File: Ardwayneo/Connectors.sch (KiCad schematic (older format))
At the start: 4 parts

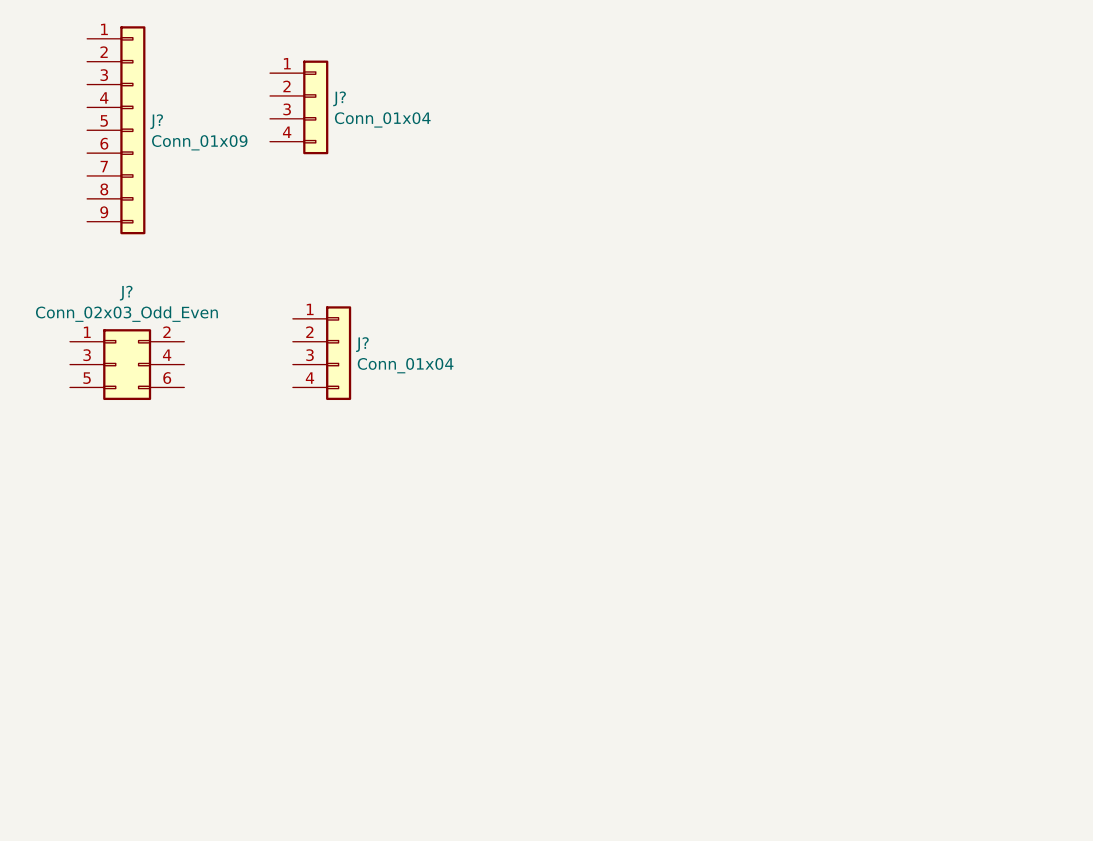
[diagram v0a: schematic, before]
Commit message: Annotation
Annotated all symbols
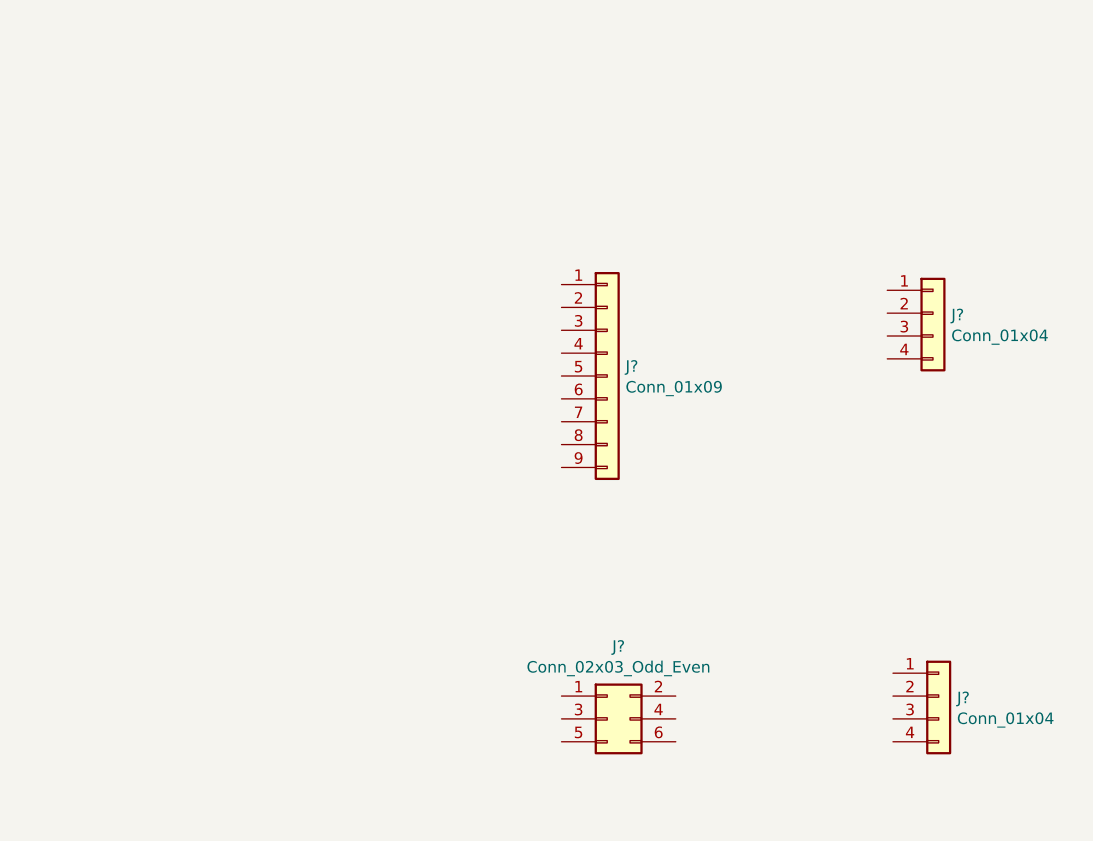
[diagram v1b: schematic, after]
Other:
- moved on the sheet: J?
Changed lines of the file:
@@
 L Connector_Generic:Conn_01x09 J?
 U 1 1 5FF1DD56
-P 3025 2225
-F 0 "J?" H 3105 2267 50  0000 L CNN
-F 1 "Conn_01x09" H 3105 2176 50  0000 L CNN
-F 2 "" H 3025 2225 50  0001 C CNN
-F 3 "~" H 3025 2225 50  0001 C CNN
-	1    3025 2225
+P 5100 3300
+F 0 "J?" H 5180 3342 50  0000 L CNN
+F 1 "Conn_01x09" H 5180 3251 50  0000 L CNN
+F 2 "" H 5100 3300 50  0001 C CNN
+F 3 "~" H 5100 3300 50  0001 C CNN
+	1    5100 3300
 	1    0    0    -1
 $EndComp
@@
 L Connector_Generic:Conn_01x04 J?
 U 1 1 5FF1EB6D
-P 3825 2075
-F 0 "J?" H 3905 2067 50  0000 L CNN
-F 1 "Conn_01x04" H 3905 1976 50  0000 L CNN
-F 2 "" H 3825 2075 50  0001 C CNN
-F 3 "~" H 3825 2075 50  0001 C CNN
-	1    3825 2075
+P 6525 3025
+F 0 "J?" H 6605 3017 50  0000 L CNN
+F 1 "Conn_01x04" H 6605 2926 50  0000 L CNN
+F 2 "" H 6525 3025 50  0001 C CNN
+F 3 "~" H 6525 3025 50  0001 C CNN
+	1    6525 3025
 	1    0    0    -1
 $EndComp
@@
 L Connector_Generic:Conn_02x03_Odd_Even J?
 U 1 1 5FF200E2
-P 2950 3250
-F 0 "J?" H 3000 3567 50  0000 C CNN
-F 1 "Conn_02x03_Odd_Even" H 3000 3476 50  0000 C CNN
-F 2 "" H 2950 3250 50  0001 C CNN
-F 3 "~" H 2950 3250 50  0001 C CNN
-	1    2950 3250
+P 5100 4800
+F 0 "J?" H 5150 5117 50  0000 C CNN
+F 1 "Conn_02x03_Odd_Even" H 5150 5026 50  0000 C CNN
+F 2 "" H 5100 4800 50  0001 C CNN
+F 3 "~" H 5100 4800 50  0001 C CNN
+	1    5100 4800
 	1    0    0    -1
 $EndComp
@@
 L Connector_Generic:Conn_01x04 J?
 U 1 1 5FF21B9C
-P 3925 3150
-F 0 "J?" H 4005 3142 50  0000 L CNN
-F 1 "Conn_01x04" H 4005 3051 50  0000 L CNN
-F 2 "" H 3925 3150 50  0001 C CNN
-F 3 "~" H 3925 3150 50  0001 C CNN
-	1    3925 3150
+P 6550 4700
+F 0 "J?" H 6630 4692 50  0000 L CNN
+F 1 "Conn_01x04" H 6630 4601 50  0000 L CNN
+F 2 "" H 6550 4700 50  0001 C CNN
+F 3 "~" H 6550 4700 50  0001 C CNN
+	1    6550 4700
 	1    0    0    -1
 $EndComp

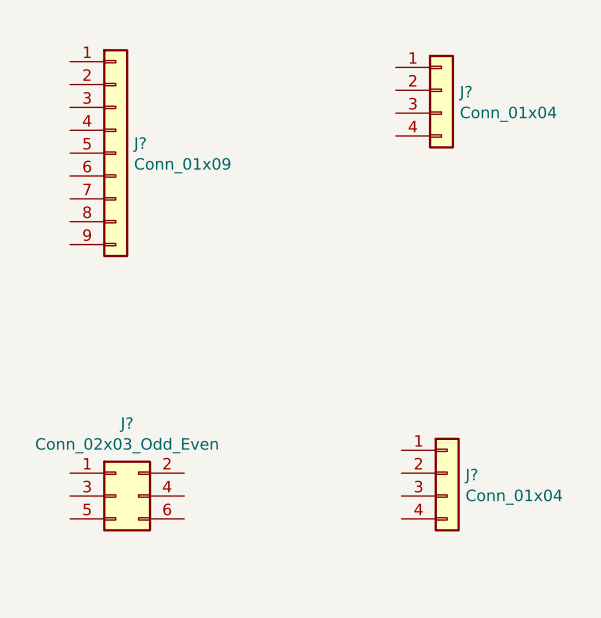
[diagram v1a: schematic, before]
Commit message: Added sheet connector pins to ATMEGA
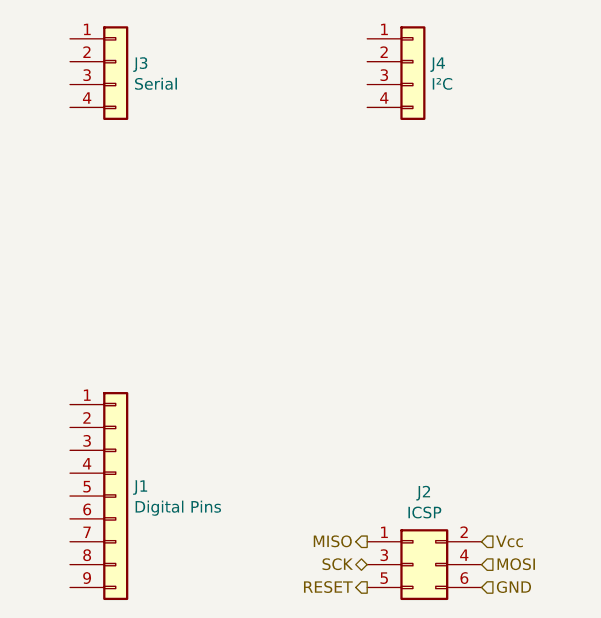
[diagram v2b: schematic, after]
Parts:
- J1: renamed from J?; value Conn_01x09 -> Digital Pins; footprint (none) -> Connector_PinHeader_2.54mm:PinHeader_1x09_P2.54mm_Vertical
- J2: renamed from J?; value Conn_02x03_Odd_Even -> ICSP; footprint (none) -> Connector_PinSocket_2.54mm:PinSocket_2x03_P2.54mm_Vertical
- J3: renamed from J?; value Conn_01x04 -> Serial; footprint (none) -> Connector_PinSocket_2.54mm:PinSocket_1x04_P2.54mm_Vertical
- J4: renamed from J?; value Conn_01x04 -> I²C; footprint (none) -> Connector_PinSocket_2.54mm:PinSocket_1x04_P2.54mm_Vertical
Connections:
- net MISO: now reaches J2.1 (Pin_1)
- net Vcc: now reaches J2.2 (Pin_2)
- net SCK: now reaches J2.3 (Pin_3)
- net MOSI: now reaches J2.4 (Pin_4)
- net RESET: now reaches J2.5 (Pin_5)
- net GND: now reaches J2.6 (Pin_6)
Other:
- moved on the sheet: J1, J2, J3, J4
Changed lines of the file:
@@
 $EndDescr
 $Comp
-L Connector_Generic:Conn_01x09 J?
+L Connector_Generic:Conn_01x09 J1
 U 1 1 5FF1DD56
-P 5100 3300
-F 0 "J?" H 5180 3342 50  0000 L CNN
-F 1 "Conn_01x09" H 5180 3251 50  0000 L CNN
-F 2 "" H 5100 3300 50  0001 C CNN
-F 3 "~" H 5100 3300 50  0001 C CNN
-	1    5100 3300
-	1    0    0    -1
-$EndComp
-$Comp
-L Connector_Generic:Conn_01x04 J?
-U 1 1 5FF1EB6D
-P 6525 3025
-F 0 "J?" H 6605 3017 50  0000 L CNN
-F 1 "Conn_01x04" H 6605 2926 50  0000 L CNN
-F 2 "" H 6525 3025 50  0001 C CNN
-F 3 "~" H 6525 3025 50  0001 C CNN
-	1    6525 3025
-	1    0    0    -1
-$EndComp
-$Comp
-L Connector_Generic:Conn_02x03_Odd_Even J?
-U 1 1 5FF200E2
 P 5100 4800
-F 0 "J?" H 5150 5117 50  0000 C CNN
-F 1 "Conn_02x03_Odd_Even" H 5150 5026 50  0000 C CNN
-F 2 "" H 5100 4800 50  0001 C CNN
+F 0 "J1" H 5180 4842 50  0000 L CNN
+F 1 "Digital Pins" H 5180 4751 50  0000 L CNN
+F 2 "Connector_PinHeader_2.54mm:PinHeader_1x09_P2.54mm_Vertical" H 5100 4800 50  0001 C CNN
 F 3 "~" H 5100 4800 50  0001 C CNN
 	1    5100 4800
@@
 $EndComp
 $Comp
-L Connector_Generic:Conn_01x04 J?
-U 1 1 5FF21B9C
-P 6550 4700
-F 0 "J?" H 6630 4692 50  0000 L CNN
-F 1 "Conn_01x04" H 6630 4601 50  0000 L CNN
-F 2 "" H 6550 4700 50  0001 C CNN
-F 3 "~" H 6550 4700 50  0001 C CNN
-	1    6550 4700
+L Connector_Generic:Conn_01x04 J3
+U 1 1 5FF1EB6D
+P 5100 2900
+F 0 "J3" H 5180 2892 50  0000 L CNN
+F 1 "Serial" H 5180 2801 50  0000 L CNN
+F 2 "Connector_PinSocket_2.54mm:PinSocket_1x04_P2.54mm_Vertical" H 5100 2900 50  0001 C CNN
+F 3 "~" H 5100 2900 50  0001 C CNN
+	1    5100 2900
 	1    0    0    -1
 $EndComp
+$Comp
+L Connector_Generic:Conn_02x03_Odd_Even J2
+U 1 1 5FF200E2
+P 6400 5100
+F 0 "J2" H 6450 5417 50  0000 C CNN
+F 1 "ICSP" H 6450 5326 50  0000 C CNN
+F 2 "Connector_PinSocket_2.54mm:PinSocket_2x03_P2.54mm_Vertical" H 6400 5100 50  0001 C CNN
+F 3 "~" H 6400 5100 50  0001 C CNN
+	1    6400 5100
+	1    0    0    -1
+$EndComp
+$Comp
+L Connector_Generic:Conn_01x04 J4
+U 1 1 5FF21B9C
+P 6400 2900
+F 0 "J4" H 6480 2892 50  0000 L CNN
+F 1 "I²C" H 6480 2801 50  0000 L CNN
+F 2 "Connector_PinSocket_2.54mm:PinSocket_1x04_P2.54mm_Vertical" H 6400 2900 50  0001 C CNN
+F 3 "~" H 6400 2900 50  0001 C CNN
+	1    6400 2900
+	1    0    0    -1
+$EndComp
+Text HLabel 6200 5000 0    50   Output ~ 0
+MISO
+Text HLabel 6200 5100 0    50   BiDi ~ 0
+SCK
+Text HLabel 6200 5200 0    50   Output ~ 0
+RESET
+Text HLabel 6700 5000 2    50   Input ~ 0
+Vcc
+Text HLabel 6700 5100 2    50   Input ~ 0
+MOSI
+Text HLabel 6700 5200 2    50   Input ~ 0
+GND
 $EndSCHEMATC

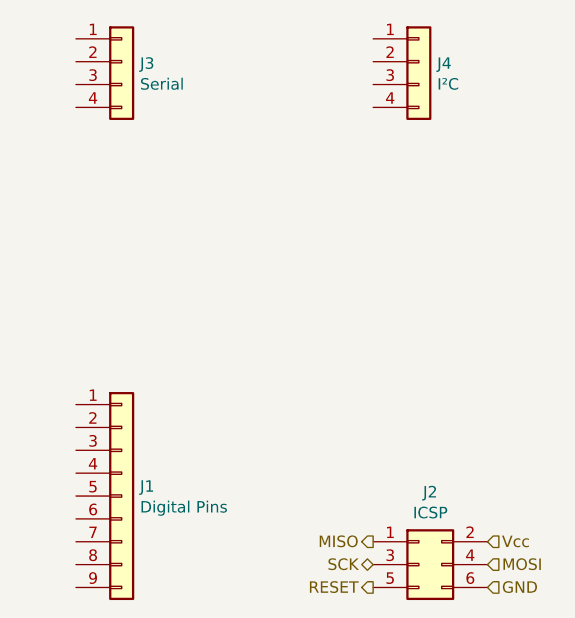
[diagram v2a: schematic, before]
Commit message: Completed wiring from connectors sheet
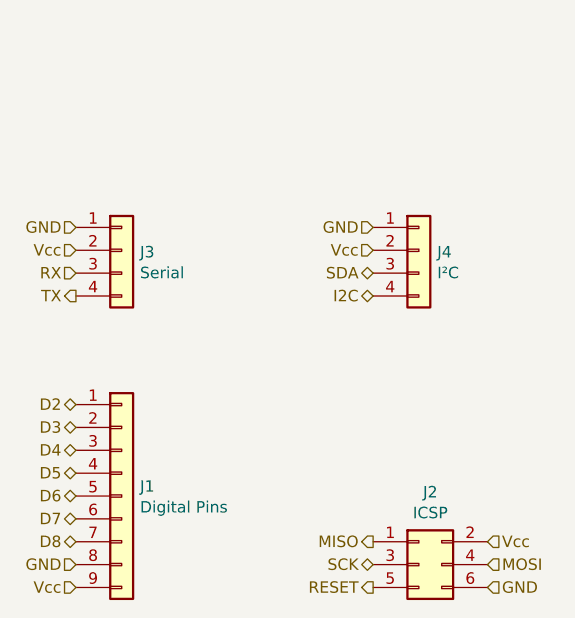
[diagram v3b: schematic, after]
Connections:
- net GND: now also J1.8 (Pin_8), J3.1 (Pin_1), J4.1 (Pin_1)
- net Vcc: now also J1.9 (Pin_9), J3.2 (Pin_2), J4.2 (Pin_2)
- net D2: now reaches J1.1 (Pin_1)
- net D3: now reaches J1.2 (Pin_2)
- net D4: now reaches J1.3 (Pin_3)
- net D5: now reaches J1.4 (Pin_4)
- net D6: now reaches J1.5 (Pin_5)
- net D7: now reaches J1.6 (Pin_6)
- net D8: now reaches J1.7 (Pin_7)
- net RX: now reaches J3.3 (Pin_3)
- net TX: now reaches J3.4 (Pin_4)
- net SDA: now reaches J4.3 (Pin_3)
- net I2C: now reaches J4.4 (Pin_4)
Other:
- moved on the sheet: J3, J4
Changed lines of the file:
@@
 L Connector_Generic:Conn_01x04 J3
 U 1 1 5FF1EB6D
-P 5100 2900
-F 0 "J3" H 5180 2892 50  0000 L CNN
-F 1 "Serial" H 5180 2801 50  0000 L CNN
-F 2 "Connector_PinSocket_2.54mm:PinSocket_1x04_P2.54mm_Vertical" H 5100 2900 50  0001 C CNN
-F 3 "~" H 5100 2900 50  0001 C CNN
-	1    5100 2900
+P 5100 3725
+F 0 "J3" H 5180 3717 50  0000 L CNN
+F 1 "Serial" H 5180 3626 50  0000 L CNN
+F 2 "Connector_PinSocket_2.54mm:PinSocket_1x04_P2.54mm_Vertical" H 5100 3725 50  0001 C CNN
+F 3 "~" H 5100 3725 50  0001 C CNN
+	1    5100 3725
 	1    0    0    -1
 $EndComp
@@
 F 3 "~" H 6400 5100 50  0001 C CNN
 	1    6400 5100
-	1    0    0    -1
-$EndComp
-$Comp
-L Connector_Generic:Conn_01x04 J4
-U 1 1 5FF21B9C
-P 6400 2900
-F 0 "J4" H 6480 2892 50  0000 L CNN
-F 1 "I²C" H 6480 2801 50  0000 L CNN
-F 2 "Connector_PinSocket_2.54mm:PinSocket_1x04_P2.54mm_Vertical" H 6400 2900 50  0001 C CNN
-F 3 "~" H 6400 2900 50  0001 C CNN
-	1    6400 2900
 	1    0    0    -1
 $EndComp
@@
 Text HLabel 6700 5200 2    50   Input ~ 0
 GND
+Text HLabel 4900 3625 0    50   Input ~ 0
+GND
+Text HLabel 4900 3725 0    50   Input ~ 0
+Vcc
+Text HLabel 4900 3825 0    50   Input ~ 0
+RX
+Text HLabel 4900 3925 0    50   Output ~ 0
+TX
+Text HLabel 6200 3625 0    50   Input ~ 0
+GND
+Text HLabel 6200 3725 0    50   Input ~ 0
+Vcc
+Text HLabel 6200 3825 0    50   BiDi ~ 0
+SDA
+Text HLabel 6200 3925 0    50   BiDi ~ 0
+I2C
+Text HLabel 4900 4400 0    50   BiDi ~ 0
+D2
+Text HLabel 4900 4500 0    50   BiDi ~ 0
+D3
+Text HLabel 4900 4600 0    50   BiDi ~ 0
+D4
+Text HLabel 4900 4700 0    50   BiDi ~ 0
+D5
+Text HLabel 4900 4800 0    50   BiDi ~ 0
+D6
+Text HLabel 4900 4900 0    50   BiDi ~ 0
+D7
+Text HLabel 4900 5000 0    50   BiDi ~ 0
+D8
+Text HLabel 4900 5100 0    50   Input ~ 0
+GND
+Text HLabel 4900 5200 0    50   Input ~ 0
+Vcc
+$Comp
+L Connector_Generic:Conn_01x04 J4
+U 1 1 5FF21B9C
+P 6400 3725
+F 0 "J4" H 6480 3717 50  0000 L CNN
+F 1 "I²C" H 6480 3626 50  0000 L CNN
+F 2 "Connector_PinSocket_2.54mm:PinSocket_1x04_P2.54mm_Vertical" H 6400 3725 50  0001 C CNN
+F 3 "~" H 6400 3725 50  0001 C CNN
+	1    6400 3725
+	1    0    0    -1
+$EndComp
 $EndSCHEMATC

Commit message: Completed all wiring
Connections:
- net I2C is gone; now on net SCK: J4.4 (Pin_4)
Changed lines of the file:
@@
 SDA
 Text HLabel 6200 3925 0    50   BiDi ~ 0
-I2C
+SCK
 Text HLabel 4900 4400 0    50   BiDi ~ 0
 D2

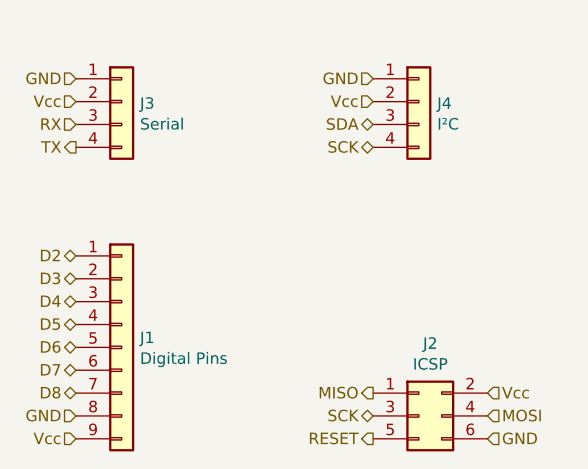
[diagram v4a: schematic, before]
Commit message: Added functional block descriptions
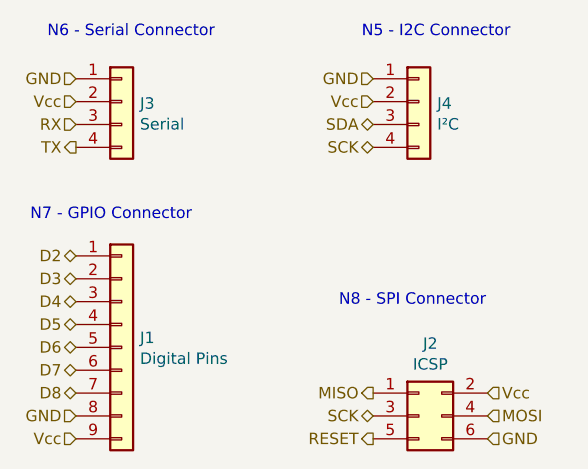
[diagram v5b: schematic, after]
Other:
- note added: "N5 - I2C Connector"
- note added: "N6 - Serial Connector"
- note added: "N7 - GPIO Connector"
- note added: "N8 - SPI Connector"
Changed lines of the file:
@@
 	1    0    0    -1
 $EndComp
+Text Notes 4775 3450 0    50   ~ 0
+N6 - Serial Connector
+Text Notes 6150 3450 0    50   ~ 0
+N5 - I2C Connector
+Text Notes 4700 4250 0    50   ~ 0
+N7 - GPIO Connector
+Text Notes 6050 4625 0    50   ~ 0
+N8 - SPI Connector
 $EndSCHEMATC
